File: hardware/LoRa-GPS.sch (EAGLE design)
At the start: 31 parts, among them J2 CON-SMA-EDGE-S, J3 USB3085-XX-X_REVD, Q1 IRLML6402, U1 MCP1703-3302E/CB, Y1 CRYSTAL.ABS07

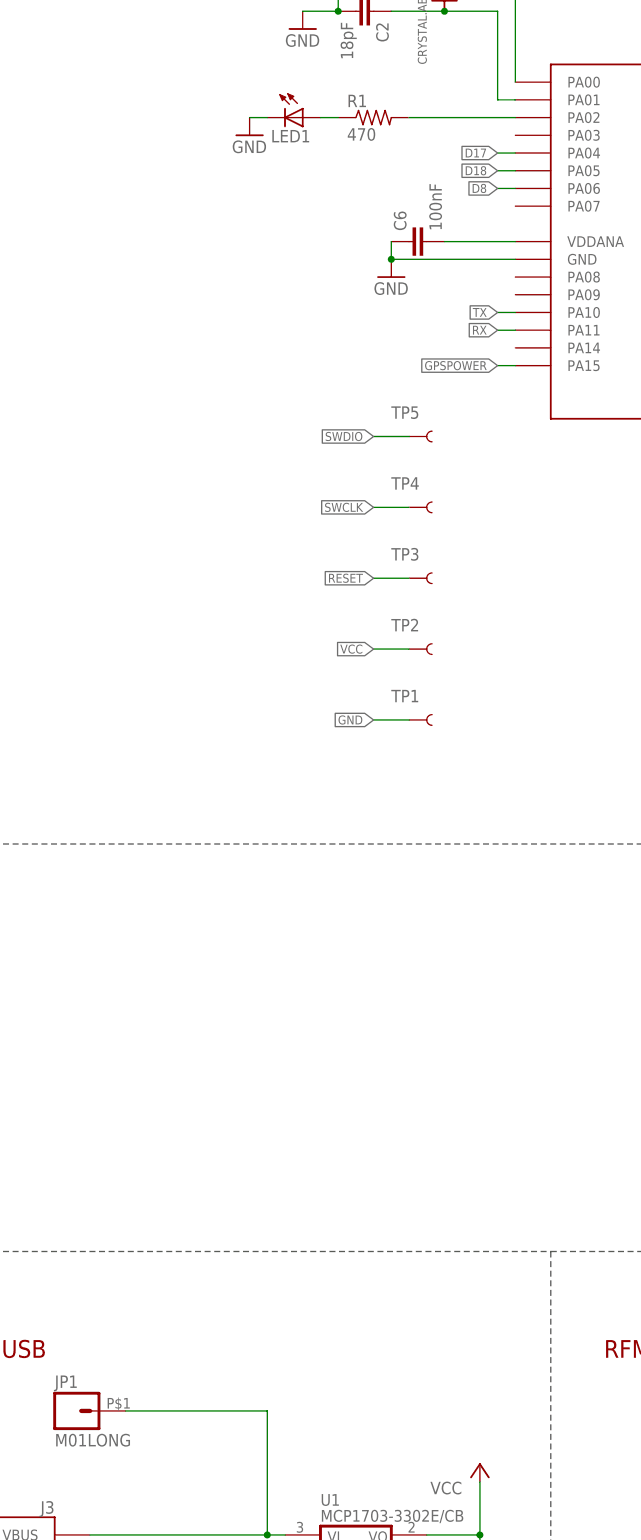
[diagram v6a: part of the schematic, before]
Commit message: bat mon. DRC keepout issue
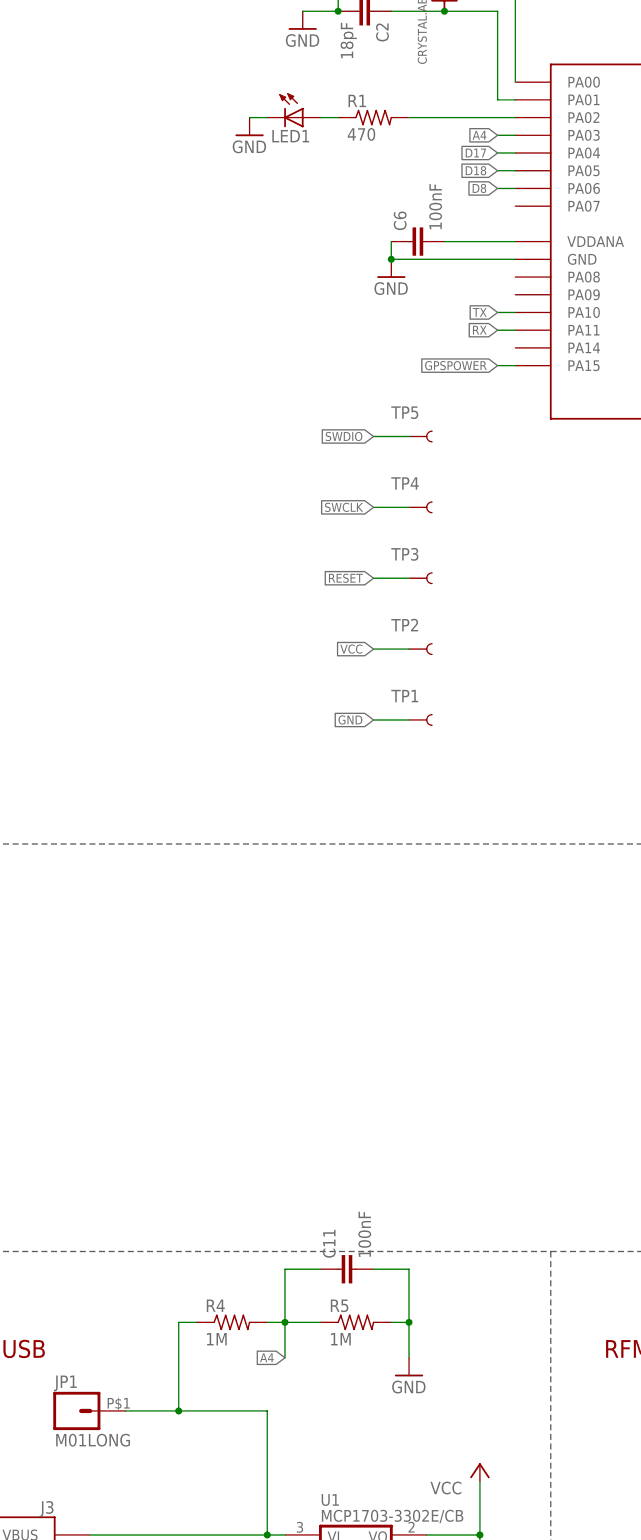
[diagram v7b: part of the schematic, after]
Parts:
- added C11: 100nF, nootropicdesign:CAPC0603-THINCREAM
- added R4, R5: 1M, rcl:R-US_R0603
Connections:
- new net A4: C11.1, R4.2, R5.1, SAMD21.PA03
- net GND: now also C11.2, R5.2
- net VIN: now also R4.1
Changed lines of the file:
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@@
 <part name="J3" library="USB3085-XX-X_REVD" deviceset="USB3085-XX-X_REVD" device=""/>
 <part name="S1" library="SamacSys_Parts" deviceset="SKTHACE010" device=""/>
+<part name="R4" library="rcl" library_urn="urn:adsk.eagle:library:334" deviceset="R-US_" device="R0603" package3d_urn="urn:adsk.eagle:package:23555/3" value="1M"/>
+<part name="R5" library="rcl" library_urn="urn:adsk.eagle:library:334" deviceset="R-US_" device="R0603" package3d_urn="urn:adsk.eagle:package:23555/3" value="1M"/>
+<part name="GND17" library="supply1" deviceset="GND" device=""/>
+<part name="C11" library="nootropicdesign" deviceset="CAP" device="C0603-THINCREAM" value="100nF">
+<attribute name="MF" value="AVX"/>
+<attribute name="MPN" value="02016D104KAT2A"/>
+<attribute name="OC_FARNELL" value="1657913"/>
+</part>
 </parts>
 <sheets>
@@
 <attribute name="VALUE" x="-110.49" y="5.08" size="1.778" layer="96" align="center-left"/>
 </instance>
+<instance part="R4" gate="G$1" x="-241.3" y="-86.36" smashed="yes">
+<attribute name="NAME" x="-245.11" y="-84.8614" size="1.778" layer="95"/>
+<attribute name="VALUE" x="-245.11" y="-89.662" size="1.778" layer="96"/>
+</instance>
+<instance part="R5" gate="G$1" x="-223.52" y="-86.36" smashed="yes">
+<attribute name="NAME" x="-227.33" y="-84.8614" size="1.778" layer="95"/>
+<attribute name="VALUE" x="-227.33" y="-89.662" size="1.778" layer="96"/>
+</instance>
+<instance part="GND17" gate="1" x="-215.9" y="-93.98" smashed="yes">
+<attribute name="VALUE" x="-218.44" y="-96.52" size="1.778" layer="96"/>
+</instance>
+<instance part="C11" gate="G$1" x="-226.06" y="-78.74" smashed="yes" rot="R90">
+<attribute name="NAME" x="-226.441" y="-77.216" size="1.778" layer="95" rot="R90"/>
+<attribute name="VALUE" x="-221.361" y="-77.216" size="1.778" layer="96" rot="R90"/>
+<attribute name="OC_FARNELL" x="-226.06" y="-78.74" size="1.778" layer="96" rot="R90" display="off"/>
+<attribute name="MF" x="-226.06" y="-78.74" size="1.778" layer="96" rot="R90" display="off"/>
+<attribute name="MPN" x="-226.06" y="-78.74" size="1.778" layer="96" rot="R90" display="off"/>
+</instance>
 </instances>
 <busses>
@@
 <junction x="-106.68" y="-2.54"/>
 </segment>
+<segment>
+<pinref part="R5" gate="G$1" pin="2"/>
+<pinref part="GND17" gate="1" pin="GND"/>
+<wire x1="-218.44" y1="-86.36" x2="-215.9" y2="-86.36" width="0.1524" layer="91"/>
+<wire x1="-215.9" y1="-86.36" x2="-215.9" y2="-91.44" width="0.1524" layer="91"/>
+<pinref part="C11" gate="G$1" pin="2"/>
+<wire x1="-220.98" y1="-78.74" x2="-215.9" y2="-78.74" width="0.1524" layer="91"/>
+<wire x1="-215.9" y1="-78.74" x2="-215.9" y2="-86.36" width="0.1524" layer="91"/>
+<junction x="-215.9" y="-86.36"/>
+</segment>
 </net>
 <net name="VCC" class="0">
@@
 <wire x1="-236.22" y1="-116.84" x2="-233.68" y2="-116.84" width="0.1524" layer="91"/>
 <pinref part="JP1" gate="G$1" pin="1"/>
-<wire x1="-256.54" y1="-99.06" x2="-236.22" y2="-99.06" width="0.1524" layer="91"/>
+<wire x1="-256.54" y1="-99.06" x2="-248.92" y2="-99.06" width="0.1524" layer="91"/>
+<wire x1="-248.92" y1="-99.06" x2="-236.22" y2="-99.06" width="0.1524" layer="91"/>
 <wire x1="-236.22" y1="-99.06" x2="-236.22" y2="-116.84" width="0.1524" layer="91"/>
 <junction x="-236.22" y="-116.84"/>
 <pinref part="J3" gate="G$1" pin="VBUS"/>
+<pinref part="R4" gate="G$1" pin="1"/>
+<wire x1="-246.38" y1="-86.36" x2="-248.92" y2="-86.36" width="0.1524" layer="91"/>
+<wire x1="-248.92" y1="-86.36" x2="-248.92" y2="-99.06" width="0.1524" layer="91"/>
+<junction x="-248.92" y="-99.06"/>
 </segment>
 </net>
@@
 <wire x1="-200.66" y1="50.8" x2="-203.2" y2="50.8" width="0.1524" layer="91"/>
 <label x="-203.2" y="50.8" size="1.27" layer="95" rot="R180" xref="yes"/>
+</segment>
+</net>
+<net name="A4" class="0">
+<segment>
+<pinref part="SAMD21" gate="G$1" pin="PA03"/>
+<wire x1="-200.66" y1="83.82" x2="-203.2" y2="83.82" width="0.1524" layer="91"/>
+<label x="-203.2" y="83.82" size="1.27" layer="95" rot="R180" xref="yes"/>
+</segment>
+<segment>
+<pinref part="R4" gate="G$1" pin="2"/>
+<pinref part="R5" gate="G$1" pin="1"/>
+<wire x1="-236.22" y1="-86.36" x2="-233.68" y2="-86.36" width="0.1524" layer="91"/>
+<label x="-233.68" y="-91.44" size="1.27" layer="95" rot="R180" xref="yes"/>
+<wire x1="-233.68" y1="-86.36" x2="-228.6" y2="-86.36" width="0.1524" layer="91"/>
+<wire x1="-233.68" y1="-86.36" x2="-233.68" y2="-91.44" width="0.1524" layer="91"/>
+<junction x="-233.68" y="-86.36"/>
+<pinref part="C11" gate="G$1" pin="1"/>
+<wire x1="-233.68" y1="-86.36" x2="-233.68" y2="-78.74" width="0.1524" layer="91"/>
+<wire x1="-233.68" y1="-78.74" x2="-228.6" y2="-78.74" width="0.1524" layer="91"/>
 </segment>
 </net>
@@
 packages will not be understood (or retained) with this version.
 </note>
+<note version="8.4" severity="warning">
+Since Version 8.4, EAGLE supports properties for SPICE simulation.
+Probes in schematics and SPICE mapping objects found in parts and library devices
+will not be understood with this version. Update EAGLE to the latest version
+for full support of SPICE simulation.
+</note>
 </compatibility>

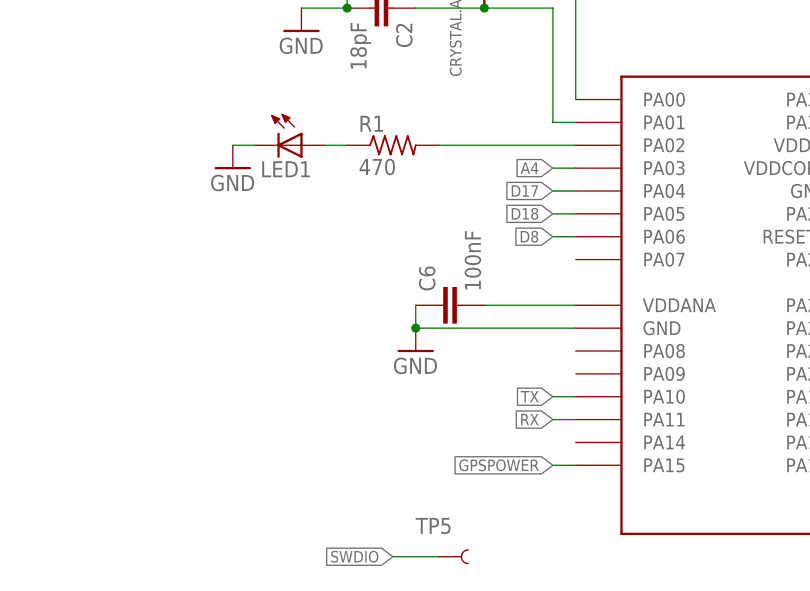
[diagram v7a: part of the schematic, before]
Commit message: add FB for VDDANA
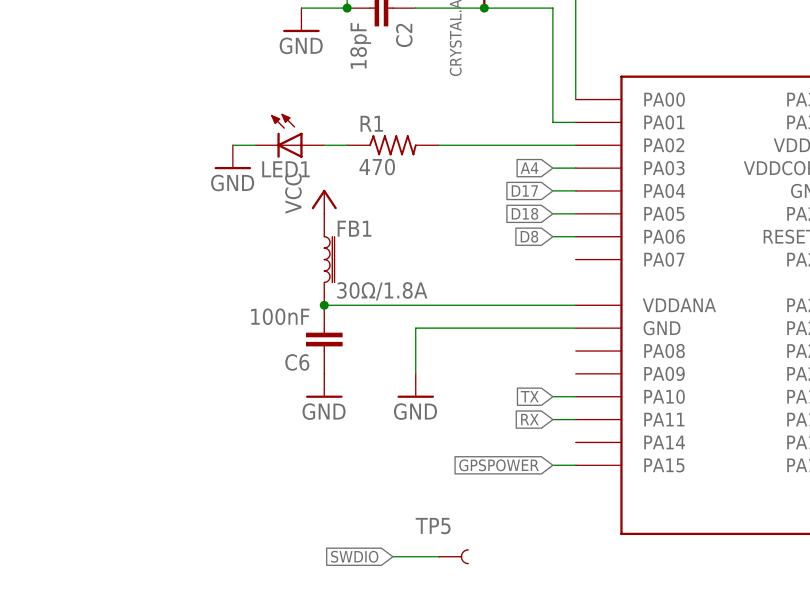
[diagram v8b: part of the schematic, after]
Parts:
- added FB1: 30Ω/1.8A, SparkFun-Coils:FERRITE_BEAD-0603
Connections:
- net N$1: now also FB1.2
- net VCC: now also FB1.1
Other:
- moved on the sheet: C6
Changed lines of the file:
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@@
 <attribute name="OC_FARNELL" value="1657913"/>
 </part>
+<part name="FB1" library="SparkFun-Coils" library_urn="urn:adsk.eagle:library:512" deviceset="FERRITE_BEAD" device="-0603" package3d_urn="urn:adsk.eagle:package:37574/1" value="30Ω/1.8A"/>
+<part name="P+4" library="supply1" deviceset="VCC" device=""/>
+<part name="GND18" library="supply1" deviceset="GND" device=""/>
 </parts>
 <sheets>
@@
 <attribute name="MPN" x="-127" y="76.2" size="1.778" layer="96" display="off"/>
 </instance>
-<instance part="C6" gate="G$1" x="-215.9" y="68.58" smashed="yes" rot="R90">
-<attribute name="NAME" x="-216.281" y="70.104" size="1.778" layer="95" rot="R90"/>
-<attribute name="VALUE" x="-211.201" y="70.104" size="1.778" layer="96" rot="R90"/>
-<attribute name="OC_FARNELL" x="-215.9" y="68.58" size="1.778" layer="96" display="off"/>
-<attribute name="MF" x="-215.9" y="68.58" size="1.778" layer="96" display="off"/>
-<attribute name="MPN" x="-215.9" y="68.58" size="1.778" layer="96" display="off"/>
+<instance part="C6" gate="G$1" x="-228.6" y="63.5" smashed="yes" rot="R180">
+<attribute name="NAME" x="-230.124" y="63.119" size="1.778" layer="95" rot="R180"/>
+<attribute name="VALUE" x="-230.124" y="68.199" size="1.778" layer="96" rot="R180"/>
+<attribute name="OC_FARNELL" x="-228.6" y="63.5" size="1.778" layer="96" rot="R90" display="off"/>
+<attribute name="MF" x="-228.6" y="63.5" size="1.778" layer="96" rot="R90" display="off"/>
+<attribute name="MPN" x="-228.6" y="63.5" size="1.778" layer="96" rot="R90" display="off"/>
 </instance>
 <instance part="C7" gate="G$1" x="-162.56" y="-124.46" smashed="yes" rot="R90">
@@
 <attribute name="MPN" x="-162.56" y="-124.46" size="1.778" layer="96" display="off"/>
 </instance>
-<instance part="GND4" gate="1" x="-218.44" y="63.5" smashed="yes">
-<attribute name="VALUE" x="-220.98" y="60.96" size="1.778" layer="96"/>
+<instance part="GND4" gate="1" x="-228.6" y="58.42" smashed="yes">
+<attribute name="VALUE" x="-231.14" y="55.88" size="1.778" layer="96"/>
 </instance>
 <instance part="GND5" gate="1" x="-127" y="68.58" smashed="yes">
@@
 <attribute name="MF" x="-226.06" y="-78.74" size="1.778" layer="96" rot="R90" display="off"/>
 <attribute name="MPN" x="-226.06" y="-78.74" size="1.778" layer="96" rot="R90" display="off"/>
+</instance>
+<instance part="FB1" gate="G$1" x="-228.6" y="73.66" smashed="yes">
+<attribute name="NAME" x="-227.33" y="76.2" size="1.778" layer="95" font="vector"/>
+<attribute name="VALUE" x="-227.33" y="71.12" size="1.778" layer="96" font="vector" align="top-left"/>
+</instance>
+<instance part="P+4" gate="VCC" x="-228.6" y="81.28" smashed="yes">
+<attribute name="VALUE" x="-231.14" y="78.74" size="1.778" layer="96" rot="R90"/>
+</instance>
+<instance part="GND18" gate="1" x="-218.44" y="58.42" smashed="yes">
+<attribute name="VALUE" x="-220.98" y="55.88" size="1.778" layer="96"/>
 </instance>
 </instances>
@@
 <pinref part="C6" gate="G$1" pin="1"/>
 <pinref part="GND4" gate="1" pin="GND"/>
-<wire x1="-218.44" y1="68.58" x2="-218.44" y2="66.04" width="0.1524" layer="91"/>
-<pinref part="SAMD21" gate="G$1" pin="GND@1"/>
-<wire x1="-200.66" y1="66.04" x2="-218.44" y2="66.04" width="0.1524" layer="91"/>
-<junction x="-218.44" y="66.04"/>
 </segment>
 <segment>
@@
 <junction x="-215.9" y="-86.36"/>
 </segment>
+<segment>
+<pinref part="SAMD21" gate="G$1" pin="GND@1"/>
+<wire x1="-200.66" y1="66.04" x2="-218.44" y2="66.04" width="0.1524" layer="91"/>
+<pinref part="GND18" gate="1" pin="GND"/>
+<wire x1="-218.44" y1="66.04" x2="-218.44" y2="60.96" width="0.1524" layer="91"/>
+</segment>
 </net>
 <net name="VCC" class="0">
@@
 <wire x1="-40.64" y1="-116.84" x2="-38.1" y2="-116.84" width="0.1524" layer="91"/>
 <label x="-38.1" y="-116.84" size="1.27" layer="95" xref="yes"/>
+</segment>
+<segment>
+<pinref part="FB1" gate="G$1" pin="1"/>
+<pinref part="P+4" gate="VCC" pin="VCC"/>
 </segment>
 </net>
@@
 <pinref part="C6" gate="G$1" pin="2"/>
 <pinref part="SAMD21" gate="G$1" pin="VDDANA"/>
-<wire x1="-210.82" y1="68.58" x2="-200.66" y2="68.58" width="0.1524" layer="91"/>
+<wire x1="-228.6" y1="68.58" x2="-200.66" y2="68.58" width="0.1524" layer="91"/>
+<pinref part="FB1" gate="G$1" pin="2"/>
+<junction x="-228.6" y="68.58"/>
 </segment>
 </net>
